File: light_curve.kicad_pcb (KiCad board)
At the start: 4 copper layers, 148 x 83 mm, 150 parts, among them J1 Valve Conn, J10 Valve Conn, J101 Power Input, J102 Servo, J103 Servo, J104 Servo, J105 Servo, J106 Servo, J107 Servo, J108 Servo, J109 Servo, J11 Valve Conn, J110 Servo, J111 Servo, J112 Servo, J113 Servo, J12 Valve Conn, J2 Valve Conn, J21 Power Input, J22 I2C INTERCONNECT, J23 I2C OLED, J24 POLOLU CONVERTER, J25 I2C INTERCONNECT, J26 I2C INTERCONNECT, J27 A2541WV-12P, J28 A2541WV-12P, J3 Valve Conn, J4 Valve Conn, J5 Valve Conn, J6 Valve Conn, J7 Valve Conn, J8 Valve Conn, J9 Valve Conn, Q1 AO3400A, Q10 AO3400A, Q11 AO3400A, Q12 AO3400A, Q2 AO3400A, Q3 AO3400A, Q4 AO3400A, Q5 AO3400A, Q6 AO3400A, Q7 AO3400A, Q8 AO3400A, Q9 AO3400A, SW1 SW_MEC_5G, SW2 SW_MEC_5G, SW22 CONFIG SWITCH, SW3 SW_MEC_5G, U101 USBLC6-2P6, U102 CC6920B, U103 USBLC6-2P6, U104 USBLC6-2P6, U21 TLV1117-50IDCYR, U22 SN74LVC1G07QDCKTQ1, U23 PCA9539PW_118, U24 MOUDLE-SEEEDUINO-XIAO-ESP32S3, U25 PCA9685PW, U26 LSM6DS3, U27 LIS3MDL

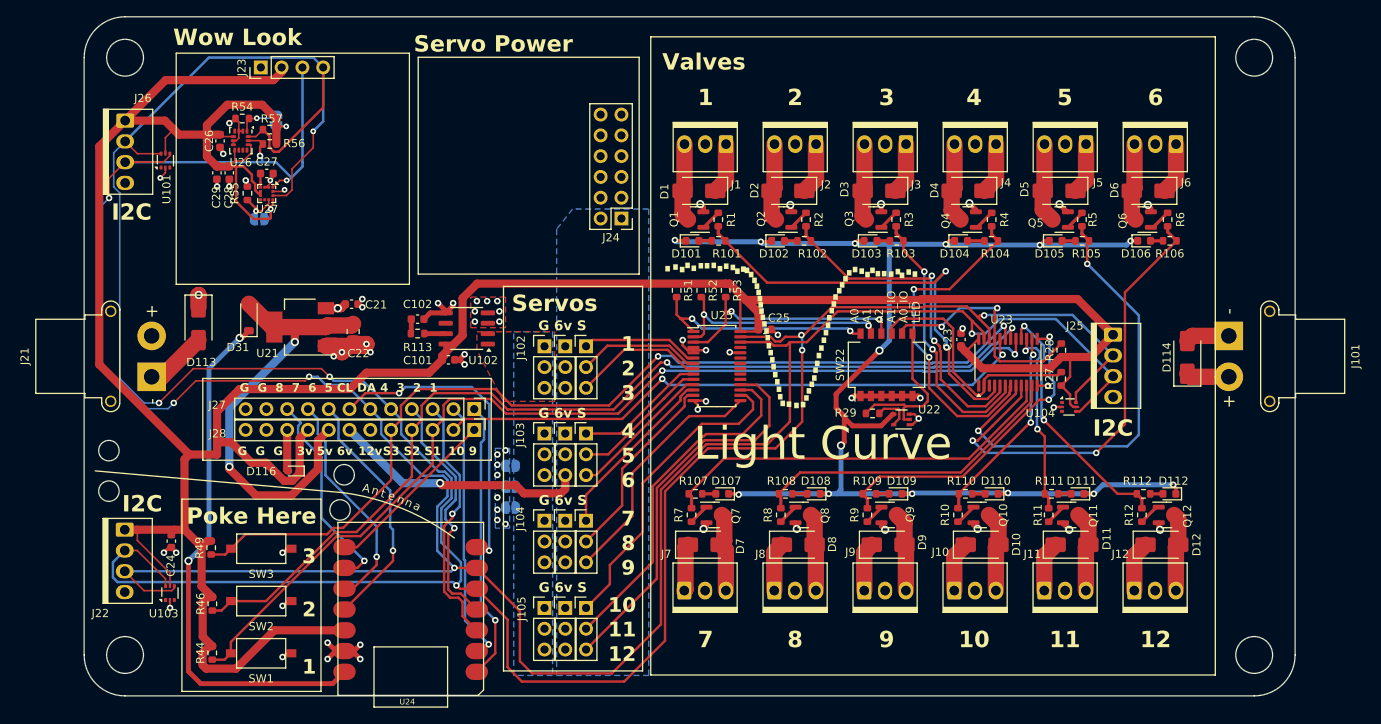
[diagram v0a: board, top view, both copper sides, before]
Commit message: Update boards for last minute order before the burn! As ordered.
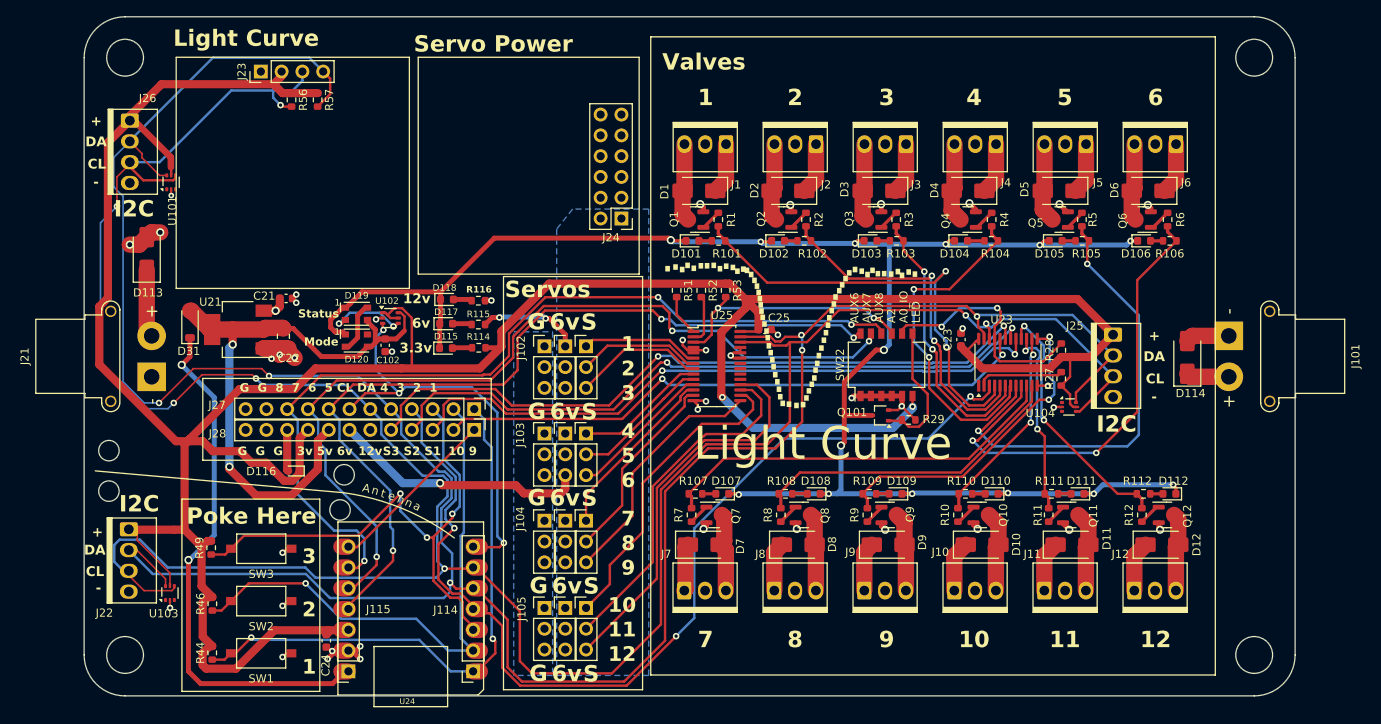
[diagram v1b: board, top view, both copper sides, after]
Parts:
- removed C101, C26, C27, C28: 0.1uF, Capacitor_SMD:C_0603_1608Metric
- removed C29: 1u, Capacitor_SMD:C_0603_1608Metric
- removed JP101, JP103, JP104, JP105, JP21: SolderJumper_2_Open, Jumper:SolderJumper-2_P1.3mm_Open_RoundedPad1.0x1.5mm
- removed R113: 10k, Resistor_SMD:R_0603_1608Metric
- removed R54, R55: 5.1k, Resistor_SMD:R_0603_1608Metric
- removed U22: SN74LVC1G07QDCKTQ1, Package_TO_SOT_SMD:SOT-353_SC-70-5
- removed U26: LSM6DS3, Package_LGA:LGA-14_3x2.5mm_P0.5mm_LayoutBorder3x4y
- removed U27: LIS3MDL, Package_LGA:LGA-12_2x2mm_P0.5mm
- added D115: LED_RED, LED_SMD:LED_0603_1608Metric, F.Cu at (120.2, 99.0)
- added D117: LED_RED, LED_SMD:LED_0603_1608Metric, F.Cu at (120.2, 96.0)
- added D118: LED_RED, LED_SMD:LED_0603_1608Metric, F.Cu at (120.3, 93.0)
- added D119: WS2812B, parts:LED_WS2812_3528_3.5x2.8mm_P1.5mm, F.Cu at (109.3, 94.8)
- added D120: WS2812B, parts:LED_WS2812_3528_3.5x2.8mm_P1.5mm, F.Cu at (109.3, 98.1)
- added J114: Conn_01x07, Connector_PinSocket_2.54mm:PinSocket_1x07_P2.54mm_Vertical, F.Cu at (123.5, 138.5)
- added J115: Conn_01x07, Connector_PinSocket_2.54mm:PinSocket_1x07_P2.54mm_Vertical, F.Cu at (108.3, 138.5)
- added Q101: AO7400-VB, Package_TO_SOT_SMD:SOT-323_SC-70, F.Cu at (173.3, 107.2)
- added R114: 130R, Resistor_SMD:R_0603_1608Metric, F.Cu at (124.2, 99.0)
- added R115: 402R, Resistor_SMD:R_0603_1608Metric, F.Cu at (124.2, 96.1)
- added R116: 1k, Resistor_SMD:R_0603_1608Metric, F.Cu at (124.2, 93.2)
- J23: value I2C OLED -> OLED
- U102: value CC6920B -> TXS0101DCKR; footprint Package_SO:SO-8_3.9x4.9mm_P1.27mm -> Package_TO_SOT_SMD:SOT-363_SC-70-6
- moved C24 22.5 mm to (105.6, 134.8)
- moved D113 10.7 mm to (83.7, 87.4), turned to 90 degrees
- moved U102 9.42 mm to (113.4, 95.3), turned to 0 degrees
- moved C22 8.54 mm to (100.3, 97.5)
- moved C21 8.03 mm to (100.7, 92.9)
- moved U21 7.61 mm to (94.8, 96.7)
- moved D31 7.25 mm to (88.9, 96.1)
- moved R57 6.89 mm to (104.5, 68.7), turned to -90 degrees
- moved R56 6.02 mm to (101.3, 68.7), turned to -90 degrees
- moved C102 5.09 mm to (112.8, 98.7), turned to -90 degrees
- moved R29 4.47 mm to (176.8, 107.8), turned to 0 degrees
- moved U101 2.74 mm to (86.6, 78.7)
- moved J26 0.58 mm to (81.9, 71.2)
- moved J22 0.50 mm to (81.8, 121.1)
- moved J23 0.50 mm to (97.6, 65.2)
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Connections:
- net Net-(D101-K) renamed /LED_GND
- C102 pad 1: GND -> +5V
- C102 pad 2: Net-(JP102-A) -> GND
- J110 pad 1: SERVO_GND -> GND
- J110 pad 2: SERVO_GND -> GND
- J110 pad 3: SERVO_GND -> GND
- J111 pad 1: SERVO_GND -> GND
- J111 pad 2: SERVO_GND -> GND
- J111 pad 3: SERVO_GND -> GND
- J112 pad 1: SERVO_GND -> GND
- J112 pad 2: SERVO_GND -> GND
- J112 pad 3: SERVO_GND -> GND
- J113 pad 1: SERVO_GND -> GND
- J113 pad 2: SERVO_GND -> GND
- J113 pad 3: SERVO_GND -> GND
- J22 pad 2: SDA -> /SDA
- J22 pad 3: SCL -> /SCL
- J23 pad 3: SCL -> /SCL
- J23 pad 4: SDA -> /SDA
- J25 pad 2: SDA -> /SDA
- J25 pad 3: SCL -> /SCL
- J26 pad 2: SDA -> /SDA
- J26 pad 3: SCL -> /SCL
- J27 pad 5: SDA -> /SDA
- J27 pad 6: SCL -> /SCL
- R29 pad 1: +3V3 -> /LED_EN
- R29 pad 2: //LED_EN -> GND
- R44 pad 1: /SW1 -> /AUX1
- R46 pad 1: /SW2 -> /AUX2
- R49 pad 1: /SW3 -> /AUX3
- R56 pad 2: SCL -> /SCL
- R57 pad 2: SDA -> /SDA
- SW1 pad 2: /SW1 -> /AUX1
- SW2 pad 2: /SW2 -> /AUX2
- SW22 pad 10: /A2 -> /AUX8
- SW22 pad 11: /A1 -> /AUX7
- SW22 pad 12: /A0 -> /AUX6
- SW22 pad 6: GND -> +3.3V
- SW22 pad 7: //LED_EN -> /LED_EN
- SW22 pad 9: /A1_IO -> /A2
- SW3 pad 2: /SW3 -> /AUX3
- U101 pad 4: SCL -> /SCL
- U101 pad 6: SDA -> /SDA
- U102 pad 1: SERVO_GND -> +3.3V
- U102 pad 2: SERVO_GND -> GND
- U102 pad 3: GND -> /AUX5
- U102 pad 4: GND -> Net-(D119-DIN)
- U102 pad 5: GND -> +3.3V
- U102 pad 6: unconnected-(U102-VZCR-Pad6) -> +5V
- U103 pad 4: SCL -> /SCL
- U103 pad 6: SDA -> /SDA
- U104 pad 4: SCL -> /SCL
- U104 pad 6: SDA -> /SDA
- U23 pad 22: SDA -> /SCL
- U23 pad 23: SCL -> /SDA
- U23 pad 3: unconnected-(U23-~RESET-Pad3) -> /AUX4
- U24 pad 5: SDA -> /SDA
- U24 pad 6: SCL -> /SCL
- U25 pad 23: unconnected-(U25-~{OE}-Pad23) -> GND
- U25 pad 25: unconnected-(U25-EXTCLK-Pad25) -> GND
- U25 pad 26: SCL -> /SCL
- U25 pad 27: SDA -> /SDA
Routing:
- net SDA: track 366.5 -> 0.00 mm, vias 7 -> 0
- net /SDA: track 0.00 -> 331.7 mm, vias 0 -> 6
- net SCL: track 331.4 -> 0.00 mm, vias 7 -> 0
- net /SCL: track 0.00 -> 327.3 mm, vias 0 -> 7
- net /AUX4: track 30.0 -> 123.4 mm, vias 1 -> 3
- net /AUX8: track 25.5 -> 108.9 mm, vias 1 -> 3
- net /AUX7: track 27.7 -> 108.5 mm, vias 1 -> 3
- net /AUX6: track 30.2 -> 104.1 mm, vias 1 -> 3
- net /LED_GND: track 165.8 -> 218.6 mm
- net /SW1: track 121.9 -> 80.1 mm
- net /SW2: track 120.0 -> 83.1 mm
- net /AUX2: track 32.3 -> 68.1 mm
- net /AUX3: track 31.4 -> 66.3 mm, vias 1 -> 3
- net /AUX1: track 34.4 -> 68.8 mm, vias 1 -> 2
- net /SW3: track 117.1 -> 85.2 mm
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- removed copper zone on F.Cu, net GND
- removed copper zone on B.Cu, net SERVO_GND
- removed copper zone on F.Cu, net SERVO_GND
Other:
- board text added: "+"
- board text added: "-"
- board text added: "3.3v"
- board text added: "6v"
- board text added: "AUX6"
- board text added: "AUX7"
- board text added: "AUX8"
- board text added: "CL"
- board text added: "DA"
- board text added: "G"
- board text added: "Made for you by Sequoia Hope Alexander with Art for Open Spaces and Sam Cooler"
- board text added: "Mode"
- board text added: "Rev 2 Aug 14 2024 wheeeee"
- board text added: "S"
- board text added: "Status"
- board text removed: "A0"
- board text removed: "A1"
- board text removed: "A1_IO"
- board text removed: "Current Sense Bypass"
- board text removed: "G 6v S"
- board text removed: "Made for you by Sequoia Sempervirens with Art for Open Spaces and Sam Cooler"
- board text removed: "Wow Look"
